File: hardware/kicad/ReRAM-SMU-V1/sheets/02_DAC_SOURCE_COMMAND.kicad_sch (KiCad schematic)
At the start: 3 parts, among them U1 AD5764 PRIMARY 5V ref LTC6655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

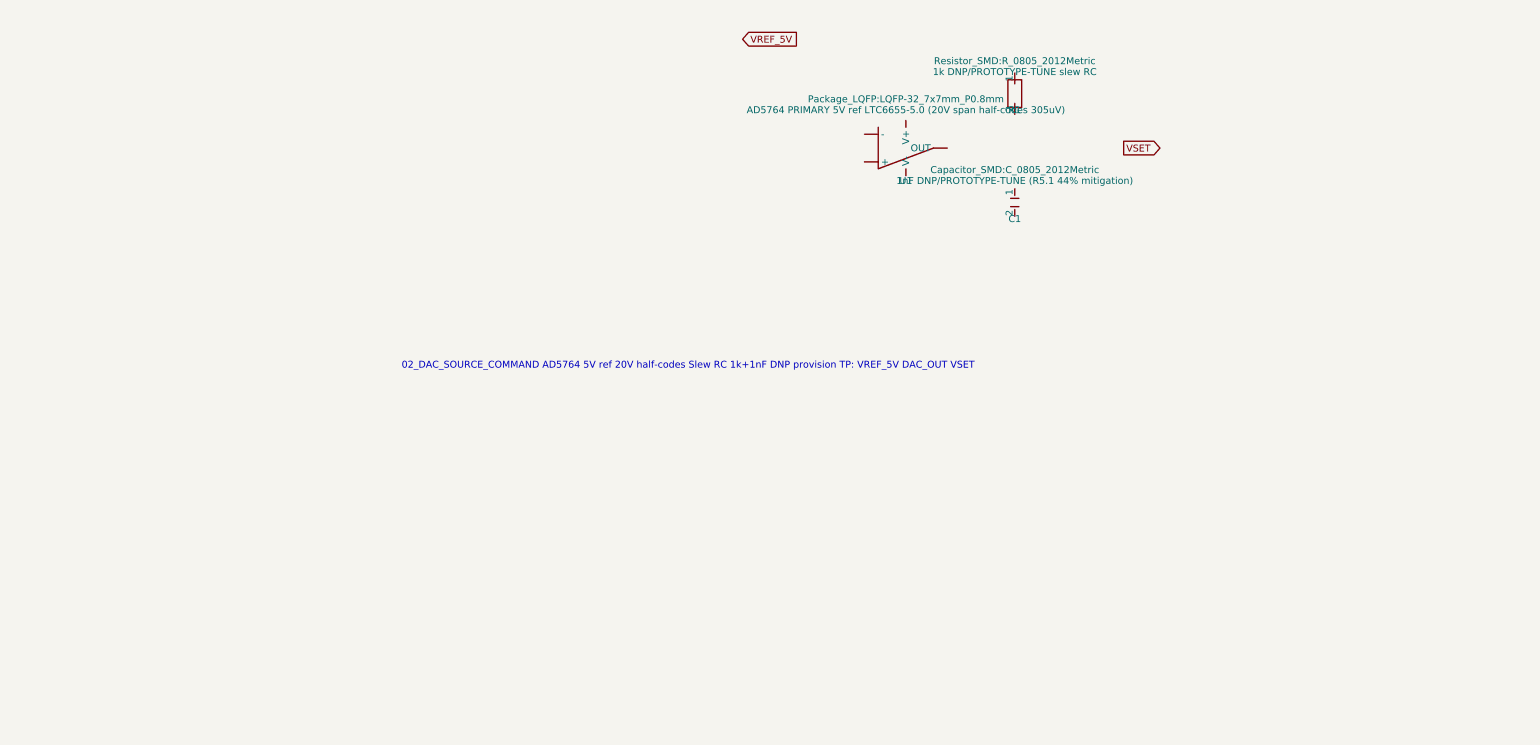
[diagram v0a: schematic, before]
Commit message: hardware: pre-ERC manufacturer corrections (LT1970 physical pins, ADS1262 TSSOP-28, MCU G431RBT6, 74LVC1G74 latch, LT5400 Kelvin, AD5764 rails, ADS1262 bipolar)
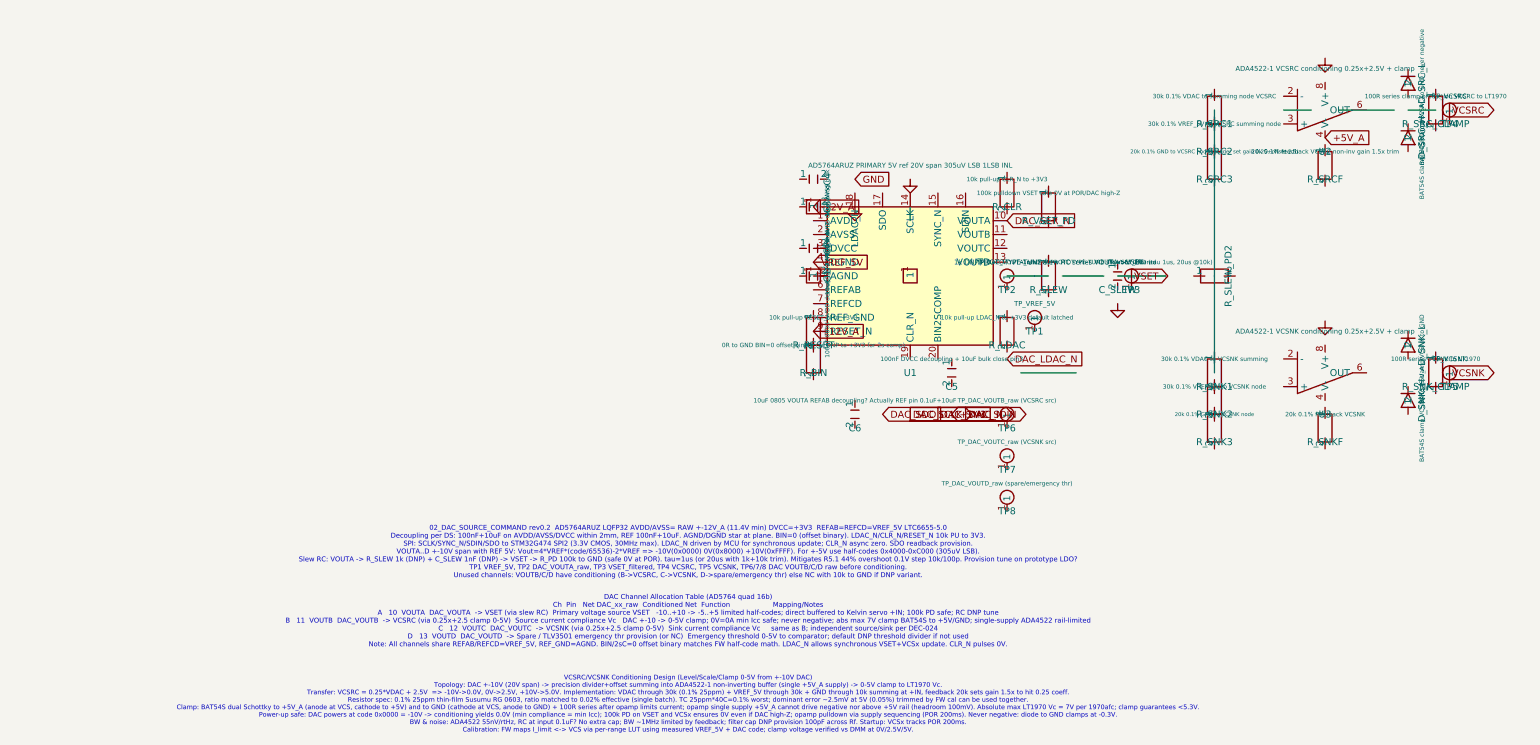
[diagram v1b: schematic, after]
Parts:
- removed R1: 1k DNP/PROTOTYPE-TUNE slew RC, Resistor_SMD:R_0805_2012Metric, symbol Device:R
- removed U1: AD5764 PRIMARY 5V ref LTC6655-5.0 (20V span half-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, Package_LQFP:LQFP-32_7x7mm_P0.8mm, symbol Device:OpAmp
- added C2: 10uF 1210 AVDD bulk, Capacitor_SMD:C_1210_3225Metric, symbol Device:C
- added C3: 100nF AVSS decoupling, Capacitor_SMD:C_0603_1608Metric, symbol Device:C
- added C4: 10uF AVSS bulk, Capacitor_SMD:C_1210_3225Metric, symbol Device:C
- added C5: 100nF DVCC decoupling + 10uF bulk close pin3, Capacitor_SMD:C_0603_1608Metric, symbol Device:C
- added C6: 10uF 0805 VOUTA REFAB decoupling? Actually REF pi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, Capacitor_SMD:C_0805_2012Metric, symbol Device:C
- added C_SLEW: 1nF DNP/PROTOTYPE-TUNE shunt to GND (tau 1us, 20u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, Capacitor_SMD:C_0805_2012Metric, symbol Device:C
- added D_SNK_H: BAT54S clamp VCSNK to +5V_A, Diode_SMD:D_SOT-23, symbol Device:D_Schottky
- added D_SNK_L: BAT54S clamp VCSNK to GND, Diode_SMD:D_SOT-23, symbol Device:D_Schottky
- added D_SRC_H: BAT54S clamp VCSRC to +5V_A, Diode_SMD:D_SOT-23, symbol Device:D_Schottky
- added D_SRC_L: BAT54S clamp VCSRC to GND never negative, Diode_SMD:D_SOT-23, symbol Device:D_Schottky
- added R_BIN: 0R to GND BIN=0 offset binary (or DNP to +3V3 for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, Resistor_SMD:R_0603_1608Metric, symbol Device:R
- added R_CLR: 10k pull-up CLR_N to +3V3, Resistor_SMD:R_0603_1608Metric, symbol Device:R
- added R_LDAC: 10k pull-up LDAC_N to +3V3 default latched, Resistor_SMD:R_0603_1608Metric, symbol Device:R
- added R_SLEW: 1k DNP/PROTOTYPE-TUNE slew RC series VOUTA->VSET, Resistor_SMD:R_0805_2012Metric, symbol Device:R
- added R_SLEW_PD2: DNP placeholder - slew RC shares VSET pulldown al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, symbol Device:R
- added R_SNK1: 30k 0.1% VDAC to VCSNK summing, Resistor_SMD:R_0603_1608Metric, symbol Device:R
- added R_SNK2: 30k 0.1% VREF_5V to VCSNK node, Resistor_SMD:R_0603_1608Metric, symbol Device:R
- added R_SNK3: 20k 0.1% GND to VCSNK node, Resistor_SMD:R_0603_1608Metric, symbol Device:R
- added R_SNKF: 20k 0.1% feedback VCSNK, Resistor_SMD:R_0603_1608Metric, symbol Device:R
- added R_SNK_CLAMP: 100R series VCSNK to LT1970, Resistor_SMD:R_0603_1608Metric, symbol Device:R
- added R_SRC1: 30k 0.1% VDAC to summing node VCSRC, Resistor_SMD:R_0603_1608Metric, symbol Device:R
- added R_SRC2: 30k 0.1% VREF_5V to VCSRC summing node, Resistor_SMD:R_0603_1608Metric, symbol Device:R
- added R_SRC3: 20k 0.1% GND to VCSRC node (divider set gain 0.25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, Resistor_SMD:R_0603_1608Metric, symbol Device:R
- added R_SRCF: 20k 0.1% feedback VCSRC non-inv gain 1.5x trim, Resistor_SMD:R_0603_1608Metric, symbol Device:R
- added R_SRC_CLAMP: 100R series clamp protection VCSRC to LT1970, Resistor_SMD:R_0603_1608Metric, symbol Device:R
- added R_VSET_PD: 100k pulldown VSET safe 0V at POR/DAC high-Z, Resistor_SMD:R_0603_1608Metric, symbol Device:R
- added TP1: TP_VREF_5V, symbol ReRAM_SMU:TestPoint
- added TP2: TP_DAC_VOUTA_raw, symbol ReRAM_SMU:TestPoint
- added TP3: TP_VSET_filtered, symbol ReRAM_SMU:TestPoint
- added TP4: TP_VCSRC, symbol ReRAM_SMU:TestPoint
- added TP5: TP_VCSNK, symbol ReRAM_SMU:TestPoint
- added TP6: TP_DAC_VOUTB_raw (VCSRC src), symbol ReRAM_SMU:TestPoint
- added TP7: TP_DAC_VOUTC_raw (VCSNK src), symbol ReRAM_SMU:TestPoint
- added TP8: TP_DAC_VOUTD_raw (spare/emergency thr), symbol ReRAM_SMU:TestPoint
- added U1: AD5764ARUZ PRIMARY 5V ref 20V span 305uV LSB 1LSB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, Package_LQFP:LQFP-32_7x7mm_P0.8mm, symbol ReRAM_SMU:AD5764
- added U2: ADA4522-1 VCSRC conditioning 0.25x+2.5V + clamp, Package_SO:SOIC-8_3.9x4.9mm_P1.27mm, symbol ReRAM_SMU:ADA4522-1
- added U3: ADA4522-1 VCSNK conditioning 0.25x+2.5V + clamp, Package_SO:SOIC-8_3.9x4.9mm_P1.27mm, symbol ReRAM_SMU:ADA4522-1
- C1: value 1nF DNP/PROTOTYPE-TUNE (R5.1 44% mitigation) -> 100nF 0603 AVDD decoupling X7R close pin1; footprint Capacitor_SMD:C_0805_2012Metric -> Capacitor_SMD:C_0603_1608Metric
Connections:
- net VREF_5V: now also U1.4 (DGND)
- new net +12V_A: U1.9 (RESET_N)
- new net +5V_A: U2.4 (V-)
- new net DAC_CLR_N: U1.10 (VOUTA)
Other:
- note added: "02_DAC_SOURCE_COMMAND rev0.2 AD5764ARUZ LQFP32 AVDD/AVSS= RAW +-12V_A (11.4V min) DVCC=+3V3 REFAB=REFCD=VREF_5V LTC6655-5.0 Decoupling per DS: 100nF+10uF on AVDD/AVSS/DVCC within 2mm, REF 100nF+10uF. AGND/DGND star at plane. BIN=0 (offset binary). LDAC_N/CLR_N/RESET_N 10k PU to 3V3. SPI: SCLK/SYNC_N/SDIN/SDO to STM32G474 SPI2 (3.3V CMOS, 30MHz max). LDAC_N driven by MCU for synchronous update; CL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"
- note added: "DAC Channel Allocation Table (AD5764 quad 16b) Ch Pin Net DAC_xx_raw Conditioned Net Function Mapping/Notes A 10 VOUTA DAC_VOUTA -> VSET (via slew RC) Primary voltage source VSET -10..+10 -> -5..+5 limited half-codes; direct buffered to Kelvin servo +IN; 100k PD safe; RC DNP tune B 11 VOUTB DAC_VOUTB -> VCSRC (via 0.25x+2.5 clamp 0-5V) Source current compliance Vc DAC +-10 -> 0-5V clamp; 0V=0A mi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"
- note added: "VCSRC/VCSNK Conditioning Design (Level/Scale/Clamp 0-5V from +-10V DAC) Topology: DAC +-10V (20V span) -> precision divider+offset summing into ADA4522-1 non-inverting buffer (single +5V_A supply) -> 0-5V clamp to LT1970 Vc. Transfer: VCSRC = 0.25*VDAC + 2.5V => -10V->0.0V, 0V->2.5V, +10V->5.0V. Implementation: VDAC through 30k (0.1% 25ppm) + VREF_5V through 30k + GND through 10k summing at +IN, 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"
- note removed: "02_DAC_SOURCE_COMMAND AD5764 5V ref 20V half-codes Slew RC 1k+1nF DNP provision TP: VREF_5V DAC_OUT VSET"

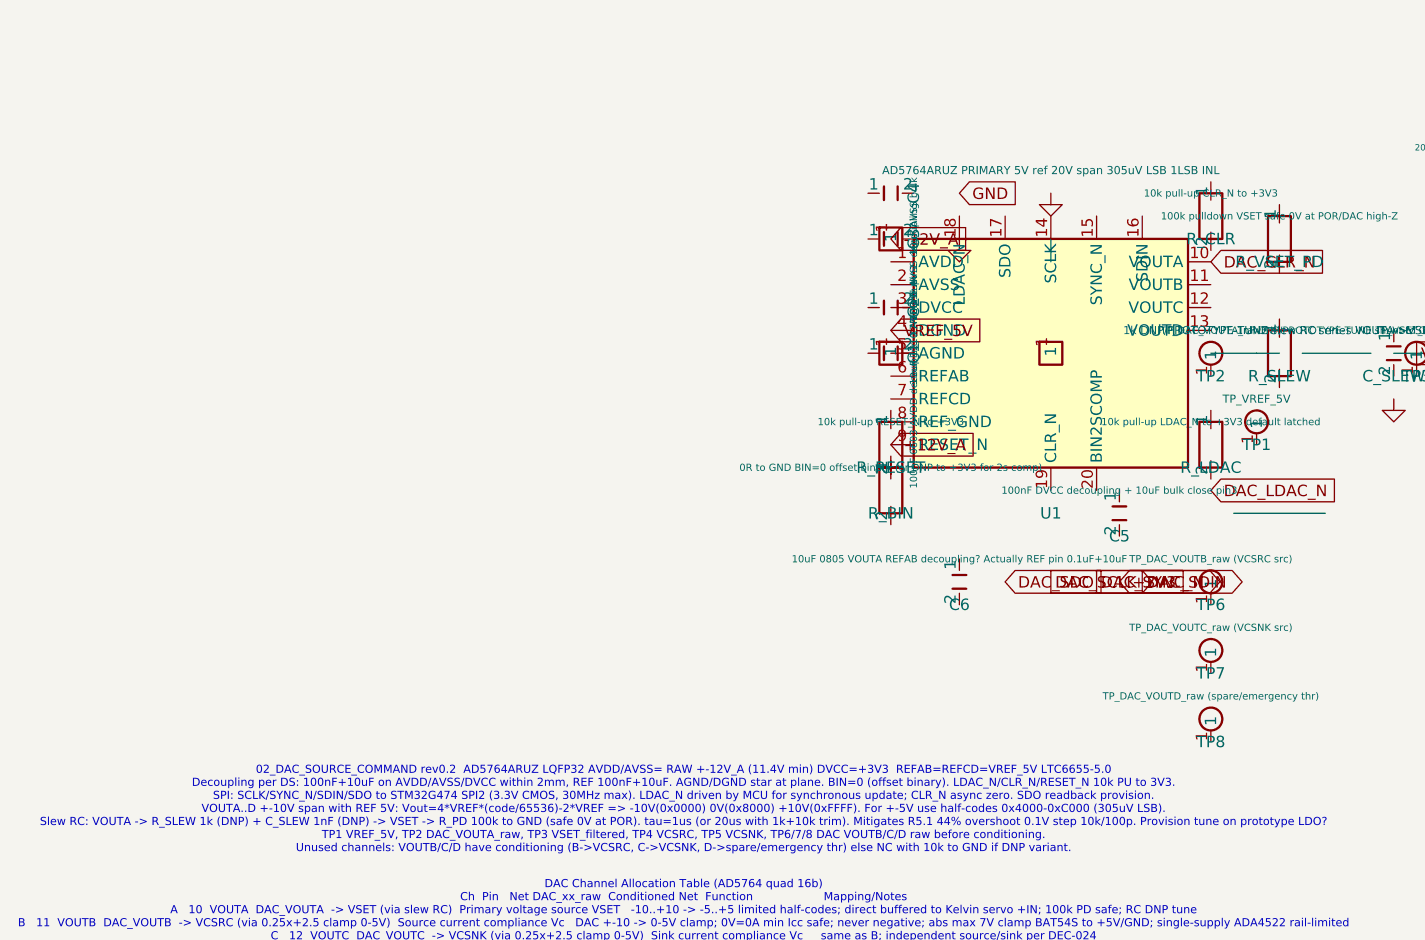
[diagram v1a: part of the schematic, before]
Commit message: hardware: pre-ERC correction gate 3 (ADS1262 Table 6-1, AD5764 32-pin C-grade, buffer 1000x fix, BAV199 after buffer, LT5400 EP floating, pin audit pass)
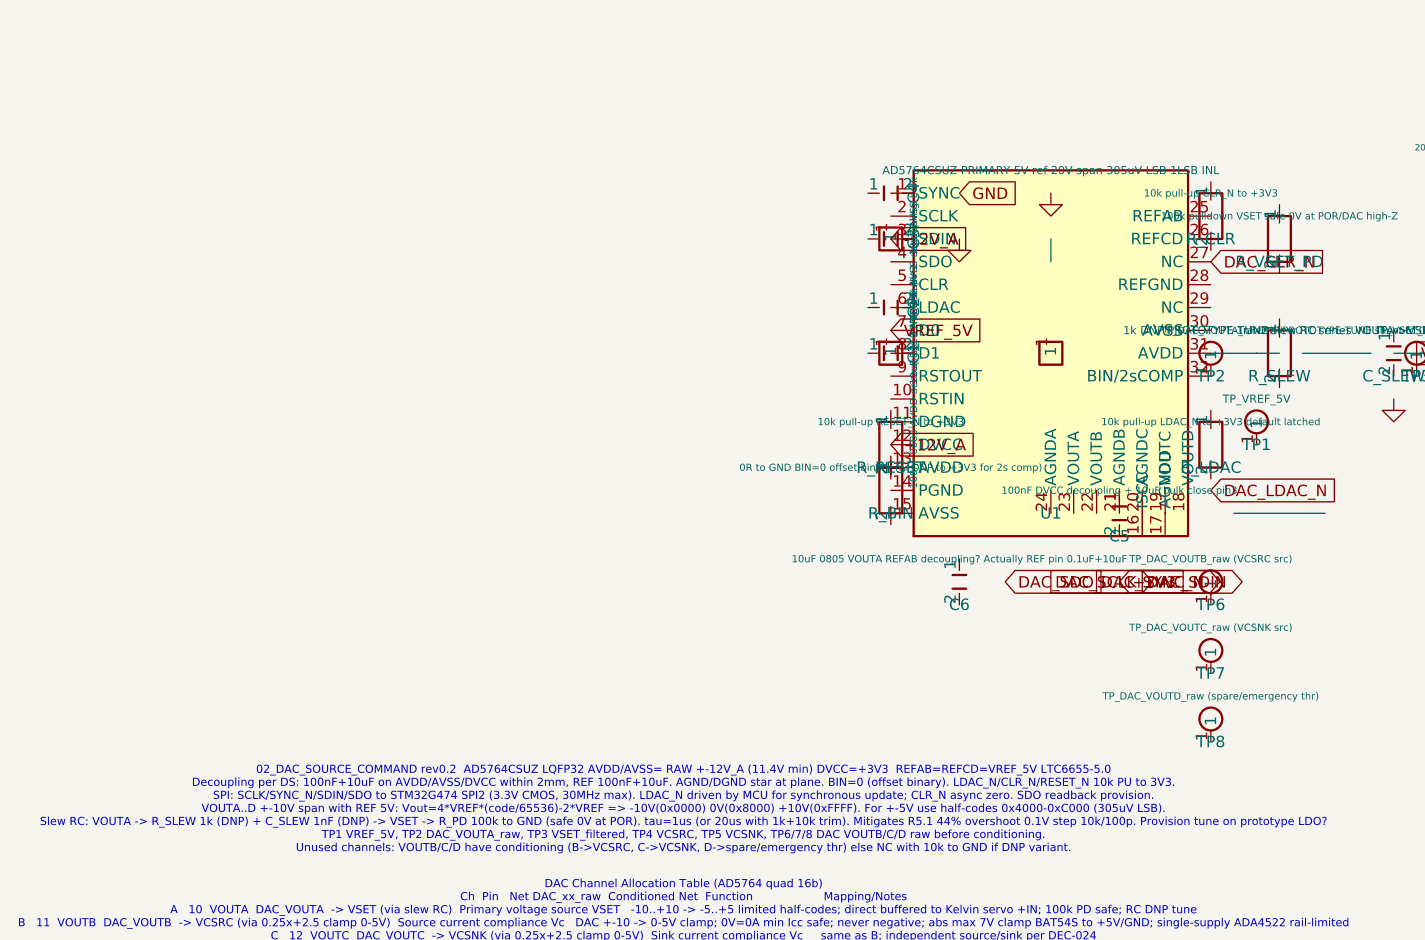
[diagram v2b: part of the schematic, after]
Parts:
- U1: value AD5764ARUZ PRIMARY 5V ref 20V span 305uV LSB 1LSB INL -> AD5764CSUZ PRIMARY 5V ref 20V span 305uV LSB 1LSB INL
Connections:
- net +12V_A: now also U1.12 (DVCC); no longer U1.9 (RESET_N)
- net -12V_A: now also U1.3 (SDIN)
- net DAC_CLR_N: now also U1.27 (NC); no longer U1.10 (VOUTA)
- net VREF_5V: now also U1.7 (D0); no longer U1.4 (DGND)
- net at TP2.1: now also U1.32 (BIN/2sCOMP)
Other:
- note added: "02_DAC_SOURCE_COMMAND rev0.2 AD5764CSUZ LQFP32 AVDD/AVSS= RAW +-12V_A (11.4V min) DVCC=+3V3 REFAB=REFCD=VREF_5V LTC6655-5.0 Decoupling per DS: 100nF+10uF on AVDD/AVSS/DVCC within 2mm, REF 100nF+10uF. AGND/DGND star at plane. BIN=0 (offset binary). LDAC_N/CLR_N/RESET_N 10k PU to 3V3. SPI: SCLK/SYNC_N/SDIN/SDO to STM32G474 SPI2 (3.3V CMOS, 30MHz max). LDAC_N driven by MCU for synchronous update; CL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"
- note removed: "02_DAC_SOURCE_COMMAND rev0.2 AD5764ARUZ LQFP32 AVDD/AVSS= RAW +-12V_A (11.4V min) DVCC=+3V3 REFAB=REFCD=VREF_5V LTC6655-5.0 Decoupling per DS: 100nF+10uF on AVDD/AVSS/DVCC within 2mm, REF 100nF+10uF. AGND/DGND star at plane. BIN=0 (offset binary). LDAC_N/CLR_N/RESET_N 10k PU to 3V3. SPI: SCLK/SYNC_N/SDIN/SDO to STM32G474 SPI2 (3.3V CMOS, 30MHz max). LDAC_N driven by MCU for synchronous update; CL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"
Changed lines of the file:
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@@
 	(symbol (lib_id "ReRAM_SMU:AD5764") (at 50.8 63.5 0) (unit 1)
 		(property "Reference" "U1" (at 50.8 81.28 0) (effects (font (size 1.27 1.27))))
-		(property "Value" "AD5764ARUZ PRIMARY 5V ref 20V span 305uV LSB 1LSB INL" (at 50.8 43.18 0) (effects (font (size 0.9 0.9))))
+		(property "Value" "AD5764CSUZ PRIMARY 5V ref 20V span 305uV LSB 1LSB INL" (at 50.8 43.18 0) (effects (font (size 0.9 0.9))))
 		(property "Footprint" "Package_LQFP:LQFP-32_7x7mm_P0.8mm" (at 50.8 41.3 0) (effects (font (size 1.27 1.27)) (hide yes)))
 	)
@@
 	(global_label "DAC_LDAC_N" (shape input) (at 68.58 78.74 0) (effects (font (size 1.27 1.27))))
 	(global_label "DAC_CLR_N" (shape input) (at 68.58 53.34 0) (effects (font (size 1.27 1.27))))
-	(text "02_DAC_SOURCE_COMMAND rev0.2  AD5764ARUZ LQFP32 AVDD/AVSS= RAW +-12V_A (11.4V min) DVCC=+3V3  REFAB=REFCD=VREF_5V LTC6655-5.0\nDecoupling per DS: 100nF+10uF on AVDD/AVSS/DVCC within 2mm, REF 100nF+10uF. AGND/DGND star at plane. BIN=0 (offset binary). LDAC_N/CLR_N/RESET_N 10k PU to 3V3.\nSPI: SCLK/SYNC_N/SDIN/SDO to STM32G474 SPI2 (3.3V CMOS, 30MHz max). LDAC_N driven by MCU for synchronous update; CLR_N async zero. SDO readback provision.\nVOUTA..D +-10V span with REF 5V: Vout=4*VREF*(code/65536)-2*VREF => -10V(0x0000) 0V(0x8000) +10V(0xFFFF). For +-5V use half-codes 0x4000-0xC000 (305uV LSB).\nSlew RC: VOUTA -> R_SLEW 1k (DNP) + C_SLEW 1nF (DNP) -> VSET -> R_PD 100k to GND (safe 0V at POR). tau=1us (or 20us with 1k+10k trim). Mitigates R5.1 44% overshoot 0.1V step 10k/100p. Provision tune on prototype LDO?\nTP1 VREF_5V, TP2 DAC_VOUTA_raw, TP3 VSET_filtered, TP4 VCSRC, TP5 VCSNK, TP6/7/8 DAC VOUTB/C/D raw before conditioning.\nUnused channels: VOUTB/C/D have conditioning (B->VCSRC, C->VCSNK, D->spare/emergency thr) else NC with 10k to GND if DNP variant." (at 10 114.3 0) (effects (font (size 0.9 0.9))))
+	(text "02_DAC_SOURCE_COMMAND rev0.2  AD5764CSUZ LQFP32 AVDD/AVSS= RAW +-12V_A (11.4V min) DVCC=+3V3  REFAB=REFCD=VREF_5V LTC6655-5.0\nDecoupling per DS: 100nF+10uF on AVDD/AVSS/DVCC within 2mm, REF 100nF+10uF. AGND/DGND star at plane. BIN=0 (offset binary). LDAC_N/CLR_N/RESET_N 10k PU to 3V3.\nSPI: SCLK/SYNC_N/SDIN/SDO to STM32G474 SPI2 (3.3V CMOS, 30MHz max). LDAC_N driven by MCU for synchronous update; CLR_N async zero. SDO readback provision.\nVOUTA..D +-10V span with REF 5V: Vout=4*VREF*(code/65536)-2*VREF => -10V(0x0000) 0V(0x8000) +10V(0xFFFF). For +-5V use half-codes 0x4000-0xC000 (305uV LSB).\nSlew RC: VOUTA -> R_SLEW 1k (DNP) + C_SLEW 1nF (DNP) -> VSET -> R_PD 100k to GND (safe 0V at POR). tau=1us (or 20us with 1k+10k trim). Mitigates R5.1 44% overshoot 0.1V step 10k/100p. Provision tune on prototype LDO?\nTP1 VREF_5V, TP2 DAC_VOUTA_raw, TP3 VSET_filtered, TP4 VCSRC, TP5 VCSNK, TP6/7/8 DAC VOUTB/C/D raw before conditioning.\nUnused channels: VOUTB/C/D have conditioning (B->VCSRC, C->VCSNK, D->spare/emergency thr) else NC with 10k to GND if DNP variant." (at 10 114.3 0) (effects (font (size 0.9 0.9))))
 	(text "DAC Channel Allocation Table (AD5764 quad 16b)\nCh  Pin   Net DAC_xx_raw  Conditioned Net  Function                    Mapping/Notes\nA   10  VOUTA  DAC_VOUTA  -> VSET (via slew RC)  Primary voltage source VSET   -10..+10 -> -5..+5 limited half-codes; direct buffered to Kelvin servo +IN; 100k PD safe; RC DNP tune\nB   11  VOUTB  DAC_VOUTB  -> VCSRC (via 0.25x+2.5 clamp 0-5V)  Source current compliance Vc   DAC +-10 -> 0-5V clamp; 0V=0A min Icc safe; never negative; abs max 7V clamp BAT54S to +5V/GND; single-supply ADA4522 rail-limited\nC   12  VOUTC  DAC_VOUTC  -> VCSNK (via 0.25x+2.5 clamp 0-5V)  Sink current compliance Vc     same as B; independent source/sink per DEC-024\nD   13  VOUTD  DAC_VOUTD  -> Spare / TLV3501 emergency thr provision (or NC)  Emergency threshold 0-5V to comparator; default DNP threshold divider if not used\nNote: All channels share REFAB/REFCD=VREF_5V, REF_GND=AGND. BIN/2sC=0 offset binary matches FW half-code math. LDAC_N allows synchronous VSET+VCSx update. CLR_N pulses 0V." (at 10 127 0) (effects (font (size 0.9 0.9))))
 	(text "VCSRC/VCSNK Conditioning Design (Level/Scale/Clamp 0-5V from +-10V DAC)\nTopology: DAC +-10V (20V span) -> precision divider+offset summing into ADA4522-1 non-inverting buffer (single +5V_A supply) -> 0-5V clamp to LT1970 Vc.\nTransfer: VCSRC = 0.25*VDAC + 2.5V  => -10V->0.0V, 0V->2.5V, +10V->5.0V. Implementation: VDAC through 30k (0.1% 25ppm) + VREF_5V through 30k + GND through 10k summing at +IN, feedback 20k sets gain 1.5x to hit 0.25 coeff.\nResistor spec: 0.1% 25ppm thin-film Susumu RG 0603, ratio matched to 0.02% effective (single batch). TC 25ppm*40C=0.1% worst; dominant error ~2.5mV at 5V (0.05%) trimmed by FW cal can be used together.\nClamp: BAT54S dual Schottky to +5V_A (anode at VCS, cathode to +5V) and to GND (cathode at VCS, anode to GND) + 100R series after opamp limits current; opamp single supply +5V_A cannot drive negative nor above +5V rail (headroom 100mV). Absolute max LT1970 Vc = 7V per 1970afc; clamp guarantees <5.3V.\nPower-up safe: DAC powers at code 0x0000 = -10V -> conditioning yields 0.0V (min compliance = min Icc); 100k PD on VSET and VCSx ensures 0V even if DAC high-Z; opamp pulldown via supply sequencing (POR 200ms). Never negative: diode to GND clamps at -0.3V.\nBW & noise: ADA4522 55nV/rtHz, RC at input 0.1uF? No extra cap; BW ~1MHz limited by feedback; filter cap DNP provision 100pF across Rf. Startup: VCSx tracks POR 200ms.\nCalibration: FW maps I_limit <-> VCS via per-range LUT using measured VREF_5V + DAC code; clamp voltage verified vs DMM at 0V/2.5V/5V." (at 10 142.24 0) (effects (font (size 0.85 0.85))))
